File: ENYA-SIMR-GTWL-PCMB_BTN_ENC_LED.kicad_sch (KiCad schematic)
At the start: 59 parts, among them J10 PICO_BLADE_1x6_MALE_RA_SMD, J11 PICO_BLADE_1x6_MALE_RA_SMD, J12 PICO_BLADE_1x14_MALE_RA_SMD, J13 PICO_BLADE_1x14_MALE_RA_SMD, J7 PICO_BLADE_1x3_MALE_RA_SMD, J8 PICO_BLADE_1x5_MALE_RA_SMD, J9 PICO_BLADE_1x5_MALE_RA_SMD, SW1 56DP30-01-1-AJN, SW2 56DP30-01-1-AJN, SW3 56DP30-01-1-AJN, SW4 56DP30-01-1-AJN

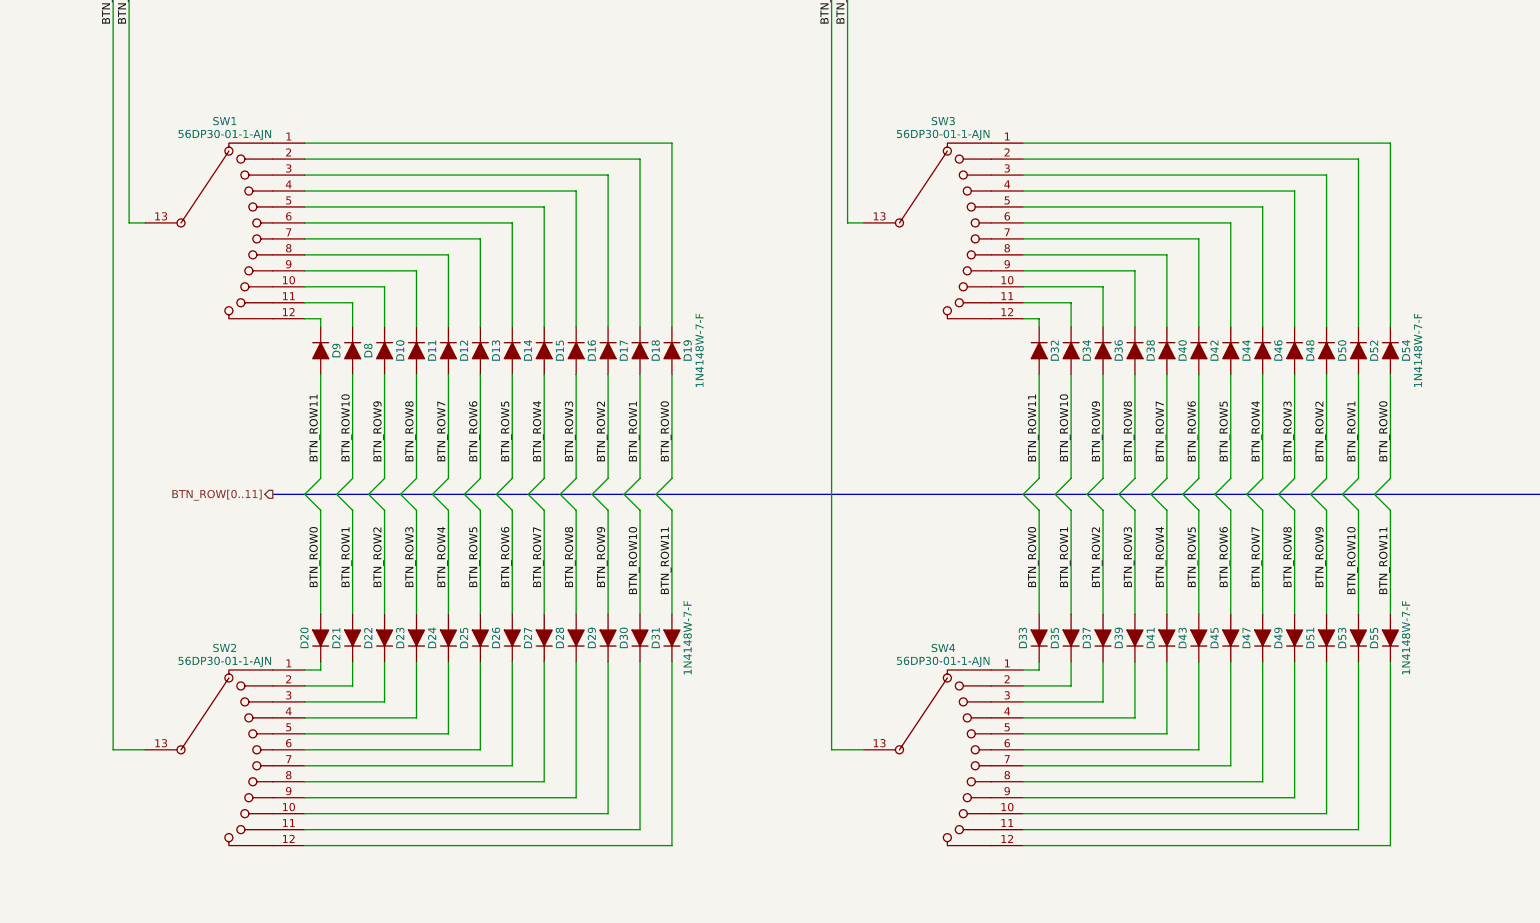
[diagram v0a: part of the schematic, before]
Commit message: using only one diode per selector switch + adding ferrite on VDDA
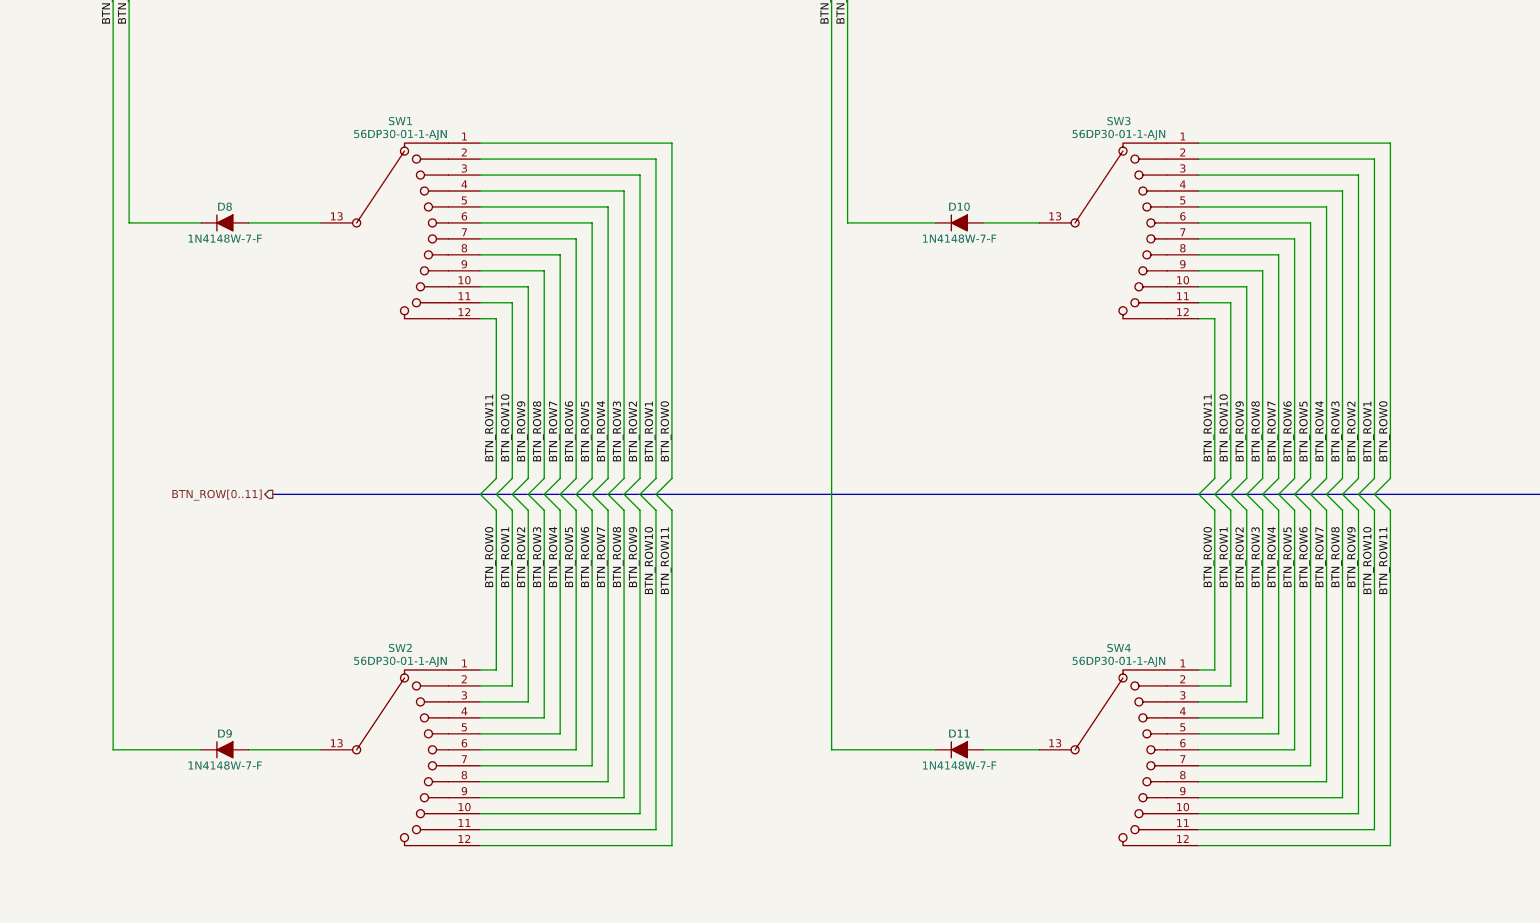
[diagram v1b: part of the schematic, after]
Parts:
- removed D12, D13, D14, D15, D16, D17, D18, D19, D20, D21, D22, D23, D24, D25, D26, D27, D28, D29, D30, D31, D32, D33, D34, D35, D36, D37, D38, D39, D40, D41, D42, D43, D44, D45, D46, D47, D48, D49, D50, D51, D52, D53, D54, D55: 1N4148W-7-F, Diode_SMD:D_SOD-123, symbol ENYA_Diode_Rectifier:1N4148W-7-F_SOD-123
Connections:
- net BTN_COL0: now also D8.1 (K); no longer SW1.13
- net BTN_COL1: now also D9.1 (K); no longer SW2.13
- net BTN_COL2: now also D10.1 (K); no longer SW3.13
- net BTN_COL3: now also D11.1 (K); no longer SW4.13
- net BTN_ROW0: now also SW1.1, SW2.1, SW3.1, SW4.1
- net BTN_ROW1: now also SW1.2, SW2.2, SW3.2, SW4.2
- net BTN_ROW10: now also SW1.11, SW2.11, SW3.11, SW4.11; no longer D8.2 (A)
- net BTN_ROW11: now also SW1.12, SW2.12, SW3.12, SW4.12; no longer D9.2 (A)
- net BTN_ROW2: now also SW1.3, SW2.3, SW3.3, SW4.3
- net BTN_ROW3: now also SW1.4, SW2.4, SW3.4, SW4.4
- net BTN_ROW4: now also SW1.5, SW2.5, SW3.5, SW4.5
- net BTN_ROW5: now also SW1.6, SW2.6, SW3.6, SW4.6
- net BTN_ROW6: now also SW1.7, SW2.7, SW3.7, SW4.7
- net BTN_ROW7: now also SW1.8, SW2.8, SW3.8, SW4.8
- net BTN_ROW8: now also SW1.9, SW2.9, SW3.9, SW4.9; no longer D11.2 (A)
- net BTN_ROW9: now also SW1.10, SW2.10, SW3.10, SW4.10; no longer D10.2 (A)
- new net: D11.2 (A), SW4.13
- new net: D9.2 (A), SW2.13
- new net: D10.2 (A), SW3.13
- new net: D8.2 (A), SW1.13
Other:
- moved on the sheet: D10, D11, D8, D9, SW1, SW2, SW3, SW4

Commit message: rework for encoder instead of selector switch
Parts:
- removed SW1, SW2, SW3, SW4: 56DP30-01-1-AJN, ENYA_Switch_Selector:56DP30-01-1-AJN_1P_12T, symbol ENYA_Switch_Selector:56DP30-01-1-AJN_1P_12T
- added C33, C34, C35, C45, C46, C47, C48, C49: 10nF_CER_0603_50V, Capacitor_SMD:C_0603_1608Metric, symbol ENYA_Cap_Smd_50V:10nF_CER_0603_50V
- added R23, R24, R25, R31, R32, R33, R34, R35, R36, R37, R38, R39, R42, R43, R44, R45: 10K_0603_100MW, Resistor_SMD:R_0603_1608Metric, symbol ENYA_Res_Smd_100mW:10K_0603_100MW
- added SW1, SW2, SW3, SW4: PEC11H-4015F-S0016, ENYA_Encoder:PEC11H_Switch_Vertical, symbol ENYA_Encoder:PEC11H-4015F-S0016
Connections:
- net +3.3V: now also R23.1, R24.2, R32.1, R33.2, R36.1, R37.2, R42.1, R43.2
- net BTN_COL0: now also J10.2 (Pin_2), J8.1 (Pin_1), SW1.S2, SW2.S2, SW3.S2, SW4.S2; no longer D8.1 (K)
- net BTN_COL1: now also J11.2 (Pin_2), J9.1 (Pin_1); no longer D9.1 (K)
- net BTN_COL2: now also J12.5 (Pin_5); no longer D10.1 (K)
- net BTN_COL3: now also J13.5 (Pin_5); no longer D11.1 (K)
- net BTN_ROW0: now also D8.2 (A), J9.2 (Pin_2); no longer J8.2 (Pin_2)
- net BTN_ROW1: now also D9.2 (A), J9.3 (Pin_3); no longer J8.3 (Pin_3)
- net BTN_ROW2: now also D10.2 (A), J9.4 (Pin_4); no longer J8.4 (Pin_4)
- net BTN_ROW3: now also D11.2 (A), J11.3 (Pin_3); no longer J9.2 (Pin_2)
- net BTN_ROW4: now also J8.2 (Pin_2); no longer J9.3 (Pin_3)
- net BTN_ROW5: now also J8.3 (Pin_3); no longer J9.4 (Pin_4)
- net BTN_ROW6: now also J8.4 (Pin_4)
- net BTN_ROW7: now also J10.3 (Pin_3)
- net GND: now also C33.2, C34.2, C35.2, C45.2, C46.2, C47.2, C48.2, C49.2, SW1.C, SW2.C, SW3.C, SW4.C
- removed net BTN_COL4: J8.1 (Pin_1), J9.1 (Pin_1)
- removed net BTN_COL5: J10.2 (Pin_2), J12.5 (Pin_5)
- removed net BTN_COL6: J11.2 (Pin_2), J13.5 (Pin_5)
- removed net BTN_ROW8: J10.3 (Pin_3), J11.3 (Pin_3)
- new net: R24.1, R25.2, SW1.A
- new net: R23.2, R31.2, SW1.B
- new net: D8.1 (K), SW1.S1
- new net: D9.1 (K), SW2.S1
- new net: R42.2, R44.2, SW3.B
- new net: R43.1, R45.2, SW3.A
- new net: D10.1 (K), SW3.S1
- new net: R37.1, R39.2, SW4.A
- new net: R36.2, R38.2, SW4.B
- new net: D11.1 (K), SW4.S1
- new net: R33.1, R35.2, SW2.A
- new net: R32.2, R34.2, SW2.B
- new net ABS_ENC_A: C47.1, R45.1
- new net ABS_ENC_B: C46.1, R44.1
- new net MAP_ENC_A: C49.1, R39.1
- new net MAP_ENC_B: C48.1, R38.1
- new net TC1_ENC_A: C45.1, R35.1
- new net TC1_ENC_B: C35.1, R34.1
- new net TC_ENC_A: C34.1, R25.1
- new net TC_ENC_B: C33.1, R31.1
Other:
- moved on the sheet: D10, D11, D8, D9
